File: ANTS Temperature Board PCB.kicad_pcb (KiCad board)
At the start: 2 copper layers, 3 parts, among them U1 RASPBERRY_PI_PICO, U2 269, U3 269

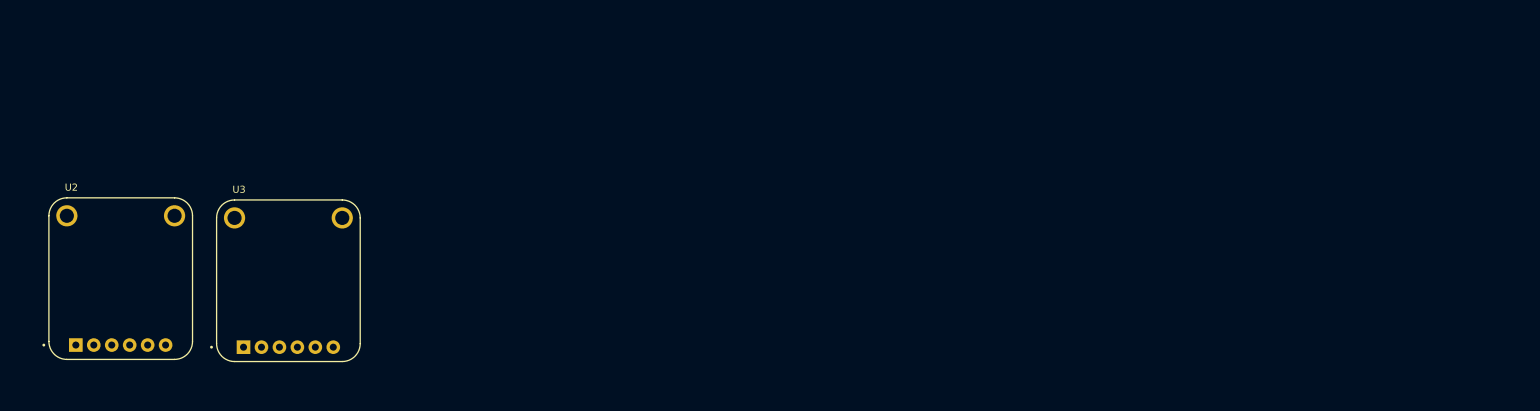
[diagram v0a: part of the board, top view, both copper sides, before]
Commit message: lil update
Added, terminal blocks and required resistors with the digikey link to blocks, and probes onto the schematic to make it easy to order
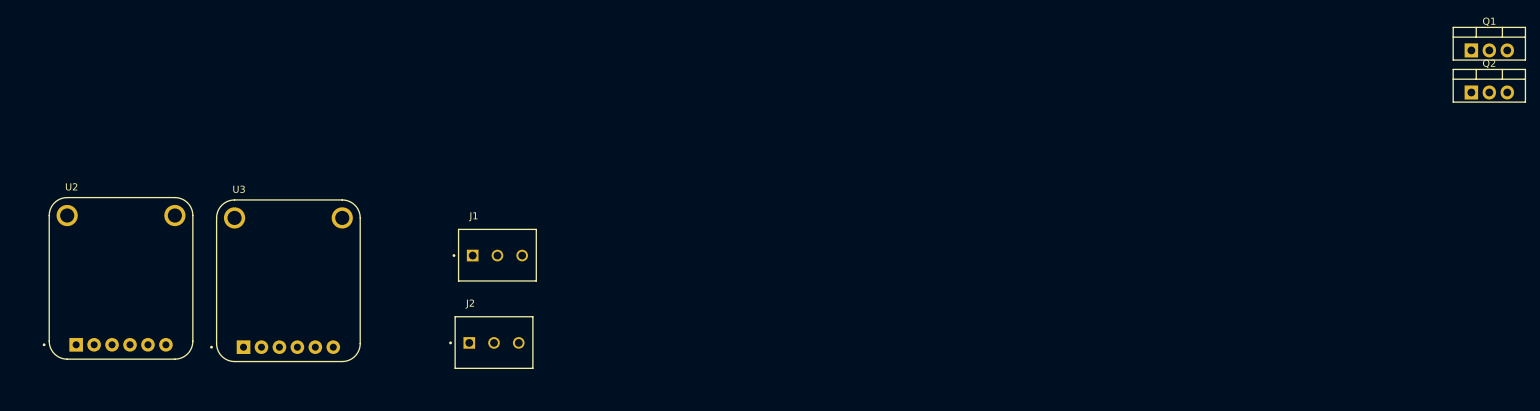
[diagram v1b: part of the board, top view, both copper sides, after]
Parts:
- added J1: 1751251, 67TERM BLOCK:PHOENIX_1751251, F.Cu at (131.3, 52.1)
- added J2: 1751251, 67TERM BLOCK:PHOENIX_1751251, F.Cu at (130.8, 64.4)
- added Q1: IRLZ34N, Package_TO_SOT_THT:TO-220-3_Vertical, F.Cu at (274.6, 19.4)
- added Q2: IRLZ34N, Package_TO_SOT_THT:TO-220-3_Vertical, F.Cu at (274.6, 25.4)
- moved U2 0.06 mm to (83.5, 51.7)
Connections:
- U1 pad 3V3: unconnected-(U1-Pad3V3) -> (no net)
- U1 pad 3V3_EN: unconnected-(U1-Pad3V3_EN) -> (no net)
- U1 pad ADC_VREF: unconnected-(U1-PadADC_VREF) -> (no net)
- U1 pad AGND: unconnected-(U1-PadAGND) -> (no net)
- U1 pad GND: unconnected-(U1-PadGND) -> (no net)
- U1 pad GND2: unconnected-(U1-PadGND2) -> (no net)
- U1 pad GND3: unconnected-(U1-PadGND3) -> (no net)
- U1 pad GND4: unconnected-(U1-PadGND4) -> (no net)
- U1 pad GND5: unconnected-(U1-PadGND5) -> (no net)
- U1 pad GND6: unconnected-(U1-PadGND6) -> (no net)
- U1 pad GND7: unconnected-(U1-PadGND7) -> (no net)
- U1 pad GP0: unconnected-(U1-PadGP0) -> (no net)
- U1 pad GP1: unconnected-(U1-PadGP1) -> (no net)
- U1 pad GP10: unconnected-(U1-PadGP10) -> (no net)
- U1 pad GP11: unconnected-(U1-PadGP11) -> (no net)
- U1 pad GP12: unconnected-(U1-PadGP12) -> (no net)
- U1 pad GP13: unconnected-(U1-PadGP13) -> (no net)
- U1 pad GP14: unconnected-(U1-PadGP14) -> (no net)
- U1 pad GP15: unconnected-(U1-PadGP15) -> (no net)
- U1 pad GP16: unconnected-(U1-PadGP16) -> (no net)
- U1 pad GP17: unconnected-(U1-PadGP17) -> (no net)
- U1 pad GP18: unconnected-(U1-PadGP18) -> (no net)
- U1 pad GP19: unconnected-(U1-PadGP19) -> (no net)
- U1 pad GP2: unconnected-(U1-PadGP2) -> (no net)
- U1 pad GP20: unconnected-(U1-PadGP20) -> (no net)
- U1 pad GP21: unconnected-(U1-PadGP21) -> (no net)
- U1 pad GP22: unconnected-(U1-PadGP22) -> (no net)
- U1 pad GP26_A0: unconnected-(U1-PadGP26_A0) -> (no net)
- U1 pad GP27_A1: unconnected-(U1-PadGP27_A1) -> (no net)
- U1 pad GP28_A2: unconnected-(U1-PadGP28_A2) -> (no net)
- U1 pad GP3: unconnected-(U1-PadGP3) -> (no net)
- U1 pad GP4: unconnected-(U1-PadGP4) -> (no net)
- U1 pad GP5: unconnected-(U1-PadGP5) -> (no net)
- U1 pad GP6: unconnected-(U1-PadGP6) -> (no net)
- U1 pad GP7: unconnected-(U1-PadGP7) -> (no net)
- U1 pad GP8: unconnected-(U1-PadGP8) -> (no net)
- U1 pad GP9: unconnected-(U1-PadGP9) -> (no net)
- U1 pad RUN: unconnected-(U1-PadRUN) -> (no net)
- U1 pad VBUS: unconnected-(U1-PadVBUS) -> (no net)
- U1 pad VSYS: unconnected-(U1-PadVSYS) -> (no net)

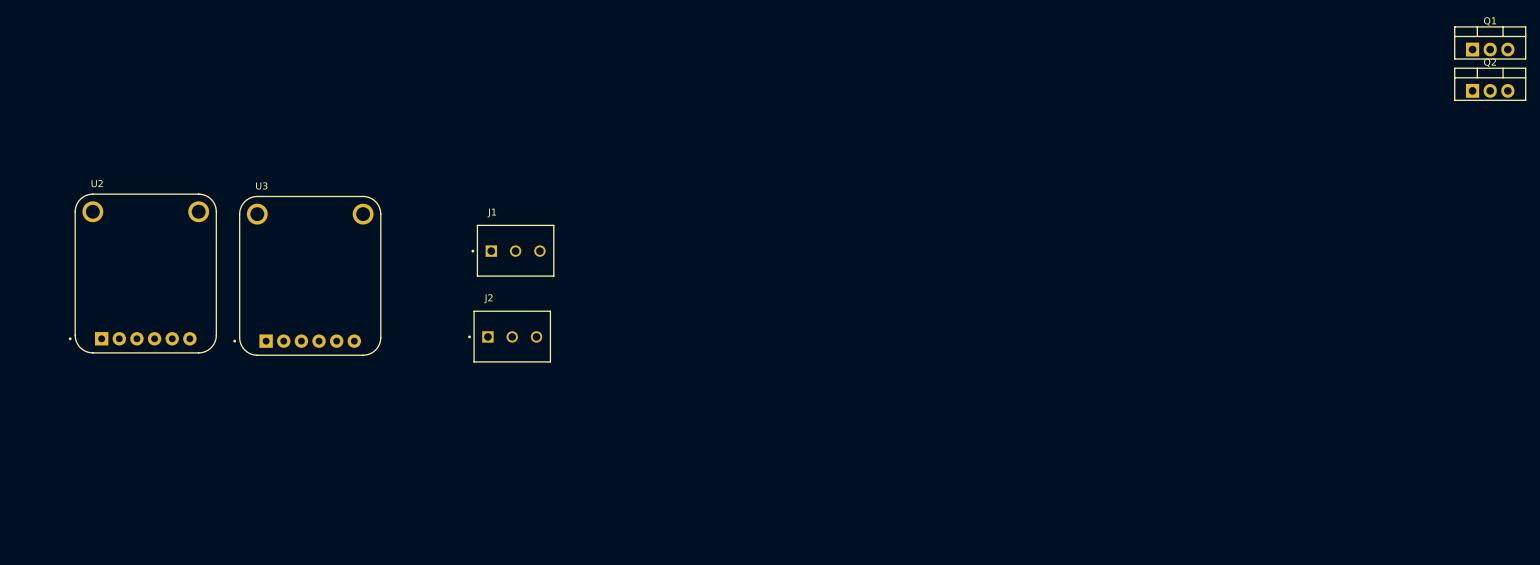
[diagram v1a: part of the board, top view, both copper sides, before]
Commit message: term block 2 pin
added 2 pin term block symbol, footprint and 3D model
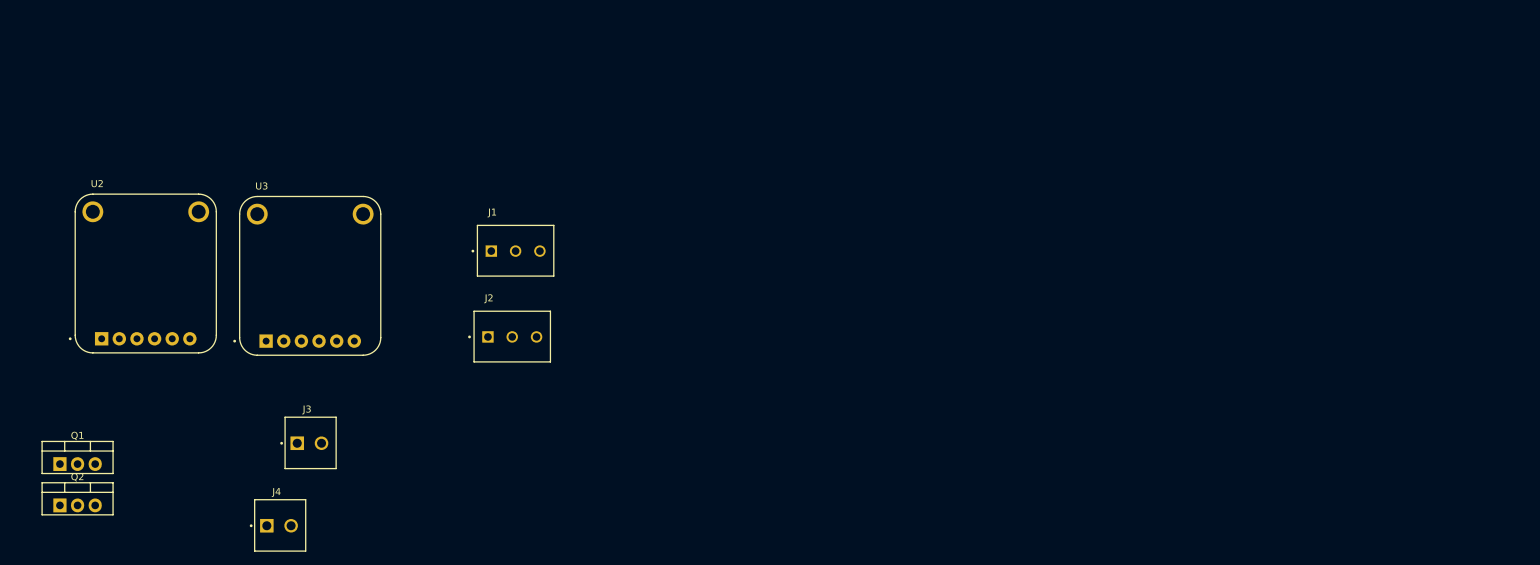
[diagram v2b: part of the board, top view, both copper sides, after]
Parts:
- added J3: EBWA-02-A, 2 PIN TERM:ADAMTECH_EBWA-02-A, F.Cu at (107.1, 76.1)
- added J4: EBWA-02-A, 2 PIN TERM:ADAMTECH_EBWA-02-A, F.Cu at (102.7, 88.0)
- moved Q1 212.0 mm to (71.2, 79.1)
- moved Q2 212.0 mm to (71.2, 85.1)
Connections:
- J1 pad 02: unconnected-(J1-SIGNAL-Pad02) -> /SIGNAL
- J1 pad 03: unconnected-(J1-PWR-Pad03) -> /PWR
- J2 pad 02: unconnected-(J2-SIGNAL-Pad02) -> /SIGNAL2
- J2 pad 03: unconnected-(J2-PWR-Pad03) -> /PWR
- U2 pad 4: unconnected-(U2-DO-Pad4) -> /DO01
- U2 pad 5: unconnected-(U2-~{CS}-Pad5) -> /CS01
- U2 pad 6: unconnected-(U2-CLK-Pad6) -> /CLK01
- U3 pad 4: unconnected-(U3-DO-Pad4) -> /DO02
- U3 pad 5: unconnected-(U3-~{CS}-Pad5) -> /CS02
- U3 pad 6: unconnected-(U3-CLK-Pad6) -> /CLK02

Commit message: No major new changes.
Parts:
- removed U2, U3: 269, ADAFRUIT:MODULE_269
- added J5: EBWA-02-A, 2 PIN TERM:ADAMTECH_EBWA-02-A, F.Cu at (132.5, 125.5)
- added J6: B2B-XH-A, B2B_XH_A (1):JST_B2B-XH-A, F.Cu at (103.0, 133.2)
- added R1: 10k, Resistor_THT:R_Axial_DIN0204_L3.6mm_D1.6mm_P7.62mm_Horizontal, F.Cu at (89.5, 131.1)
- added R2: 10k, Resistor_THT:R_Axial_DIN0204_L3.6mm_D1.6mm_P7.62mm_Horizontal, F.Cu at (89.5, 134.2)
- added R5: 4.7K, Resistor_THT:R_Axial_DIN0204_L3.6mm_D1.6mm_P7.62mm_Horizontal, F.Cu at (89.5, 137.4)
- added R6: 4.7K, Resistor_THT:R_Axial_DIN0204_L3.6mm_D1.6mm_P7.62mm_Horizontal, F.Cu at (89.5, 140.5)
- added R7: 220, Resistor_THT:R_Axial_DIN0204_L3.6mm_D1.6mm_P7.62mm_Horizontal, F.Cu at (89.5, 143.7)
- added R8: 220, Resistor_THT:R_Axial_DIN0204_L3.6mm_D1.6mm_P7.62mm_Horizontal, F.Cu at (89.5, 146.8)
- U1: footprint 2020RASPBERRY_PI_PICO:RASPBERRY_PI_PICO -> Module:RaspberryPi_Pico_Common_THT
- moved Q1 38.5 mm to (88.9, 45.0)
- moved U1 8.90 mm to (32.0, 56.5)
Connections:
- J1 pad 01: unconnected-(J1-GND-Pad01) -> GND
- J1 pad 02: /SIGNAL -> /SIGNAL1
- J1 pad 03: /PWR -> +3V3
- J2 pad 01: unconnected-(J2-GND-Pad01) -> GND
- J2 pad 03: /PWR -> +3V3
- J3 pad 1: unconnected-(J3-Pad1) -> +7.5V
- J3 pad 2: unconnected-(J3-Pad2) -> Net-(Q1-D)
- J4 pad 1: unconnected-(J4-Pad1) -> +7.5V
- J4 pad 2: unconnected-(J4-Pad2) -> Net-(J4-Drain)
- Q1 pad 1: unconnected-(Q1-G-Pad1) -> Net-(Q1-G)
- Q1 pad 2: unconnected-(Q1-D-Pad2) -> Net-(Q1-D)
- Q1 pad 3: unconnected-(Q1-S-Pad3) -> GND
- Q2 pad 1: unconnected-(Q2-G-Pad1) -> Net-(Q2-G)
- Q2 pad 2: unconnected-(Q2-D-Pad2) -> Net-(J4-Drain)
- Q2 pad 3: unconnected-(Q2-S-Pad3) -> GND

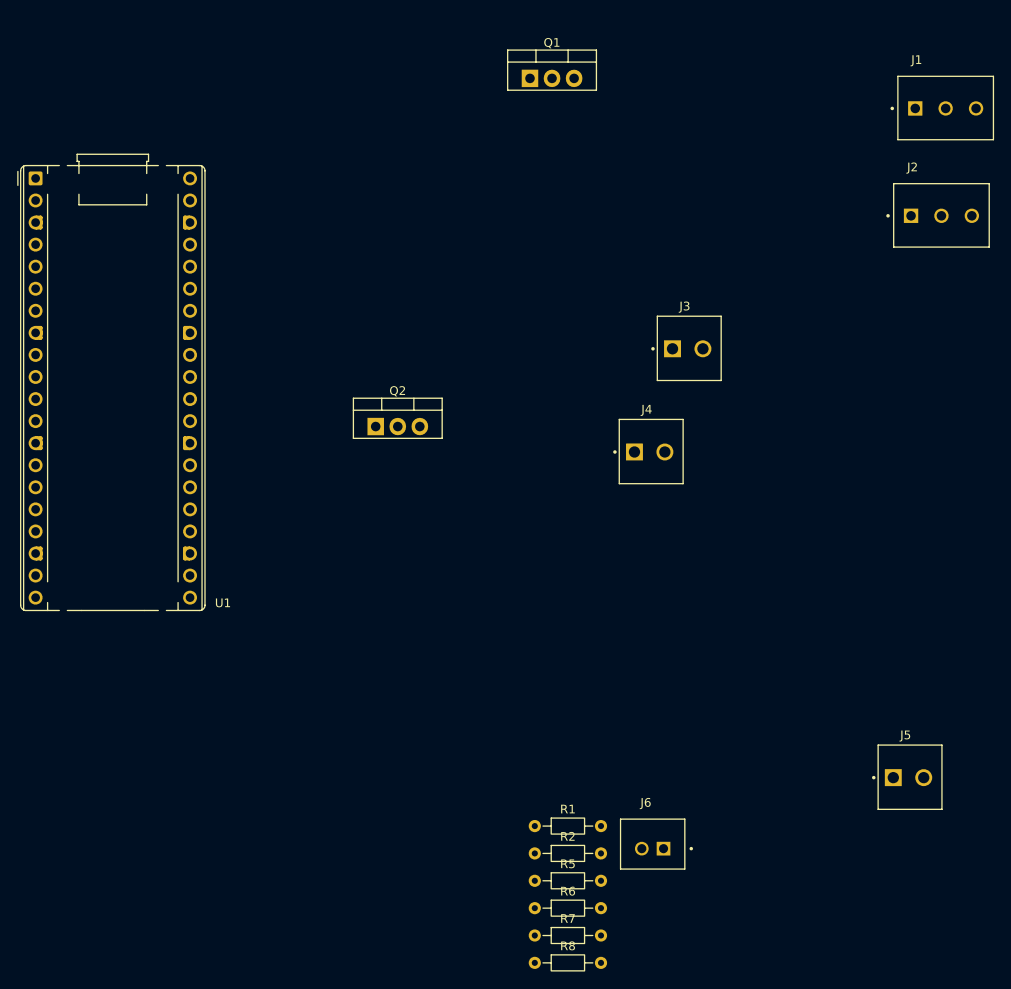
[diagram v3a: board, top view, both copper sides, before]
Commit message: Made board layout and traces. Still have to add mounting holes and silkscreen.
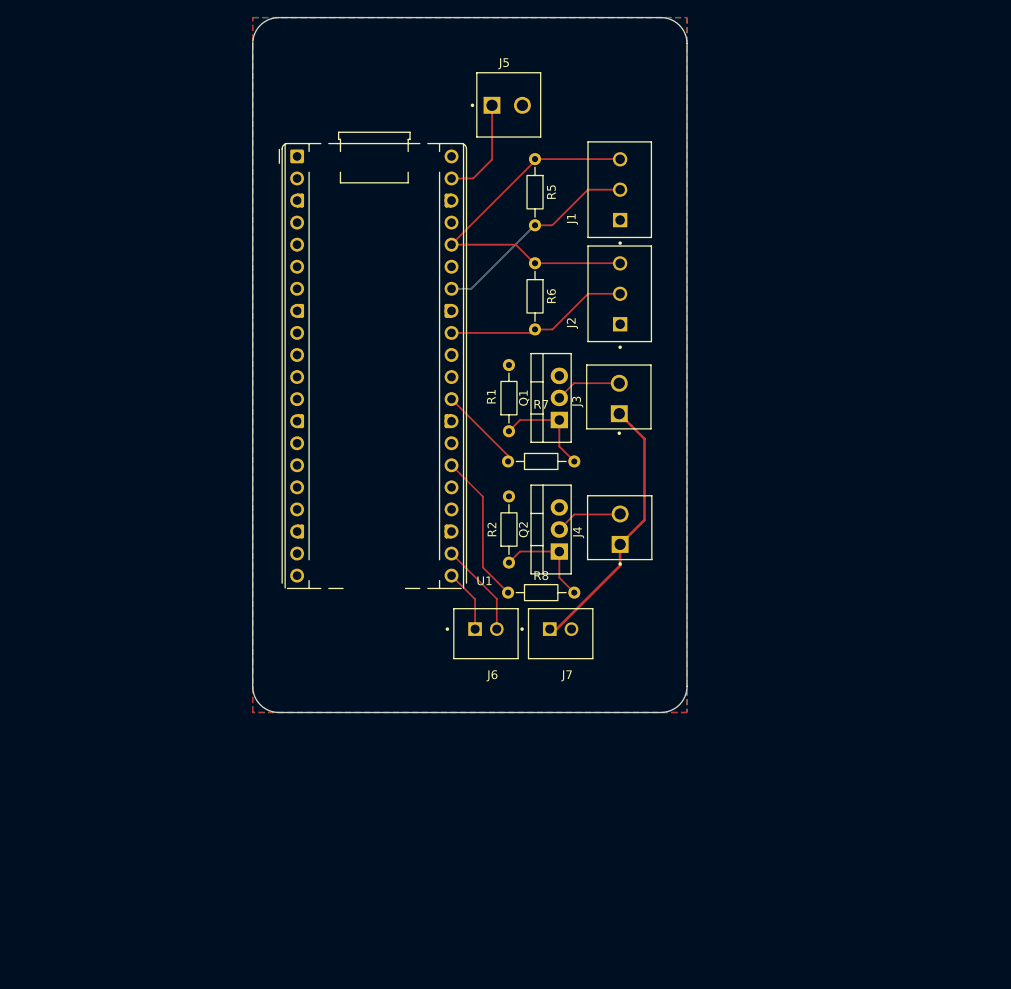
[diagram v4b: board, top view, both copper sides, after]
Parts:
- added J7: B2B-XH-A, B2B_XH_A (1):JST_B2B-XH-A, F.Cu at (92.5, 108.9)
- moved J5 90.1 mm to (86.3, 48.1)
- moved R5 83.1 mm to (89.5, 54.3), turned to -90 degrees
- moved R6 74.2 mm to (89.5, 66.3), turned to -90 degrees
- moved R7 54.7 mm to (86.4, 89.1)
- moved R1 45.6 mm to (86.5, 85.6), turned to 90 degrees
- moved R8 42.7 mm to (86.4, 104.2)
- moved Q1 39.5 mm to (92.3, 84.3), turned to 90 degrees
- moved R2 33.6 mm to (86.5, 100.7), turned to 90 degrees
- moved J6 30.9 mm to (83.8, 108.9), turned to 180 degrees
- moved J1 30.5 mm to (102.9, 63.3), turned to 90 degrees
- moved U1 30.2 mm to (62.1, 54.0)
- moved J2 29.9 mm to (102.9, 75.3), turned to 90 degrees
- moved Q2 25.6 mm to (92.3, 99.5), turned to 90 degrees
- moved J3 9.74 mm to (99.2, 81.8), turned to 90 degrees
- moved J4 9.52 mm to (99.3, 96.9), turned to 90 degrees
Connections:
- U1 pad 1: /UART_TX -> unconnected-(U1-GP0-Pad1)
- U1 pad 2: /UART_RX -> unconnected-(U1-GP1-Pad2)
- U1 pad 21: unconnected-(U1-GP16-Pad21) -> /UART_RX
- U1 pad 22: unconnected-(U1-GP17-Pad22) -> /UART_TX
- U1 pad 24: /SIGNAL2 -> unconnected-(U1-GP18-Pad24)
- U1 pad 25: /SIGNAL1 -> unconnected-(U1-GP19-Pad25)
- U1 pad 26: unconnected-(U1-GP20-Pad26) -> /mosfet2_gate
- U1 pad 29: unconnected-(U1-GP22-Pad29) -> /mosfet1_gate
- U1 pad 32: /mosfet2_gate -> /SIGNAL2
- U1 pad 34: /mosfet1_gate -> /SIGNAL1
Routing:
- net +3V3: track 0.00 -> 43.9 mm
- net +7.5V: track 0.00 -> 31.0 mm
- net /SIGNAL1: track 0.00 -> 24.1 mm
- net /SIGNAL2: track 0.00 -> 21.3 mm
- net /mosfet2_gate: track 0.00 -> 17.4 mm
- net Net-(Q1-G): track 0.00 -> 11.8 mm
- net /VSYS: track 0.00 -> 11.8 mm
- net Net-(Q2-G): track 0.00 -> 11.8 mm
- net /UART_TX: track 0.00 -> 10.9 mm
- net /mosfet1_gate: track 0.00 -> 9.87 mm
- net Net-(J4-Drain): track 0.00 -> 7.74 mm
- net Net-(Q1-D): track 0.00 -> 7.60 mm
- net /UART_RX: track 0.00 -> 7.28 mm
- added copper zone on B.Cu, net GND
- added copper zone on F.Cu, net GND
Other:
- board outline added: 50 x 80 mm
